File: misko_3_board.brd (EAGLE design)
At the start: 74 x 152 mm, 179 parts, among them IC1 ATMEGA1281-16AU, IC10 ORG1510-MK4, IC11 TPS3808G33DBVT, IC12 LTC4425, IC13 RN-42, IC14 ADXL345, IC15 74HCT1G32, IC16 FM25W256-SOIC, IC17 MICROSD_SPI_MODE, IC18 FH12-30S-0.5SH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

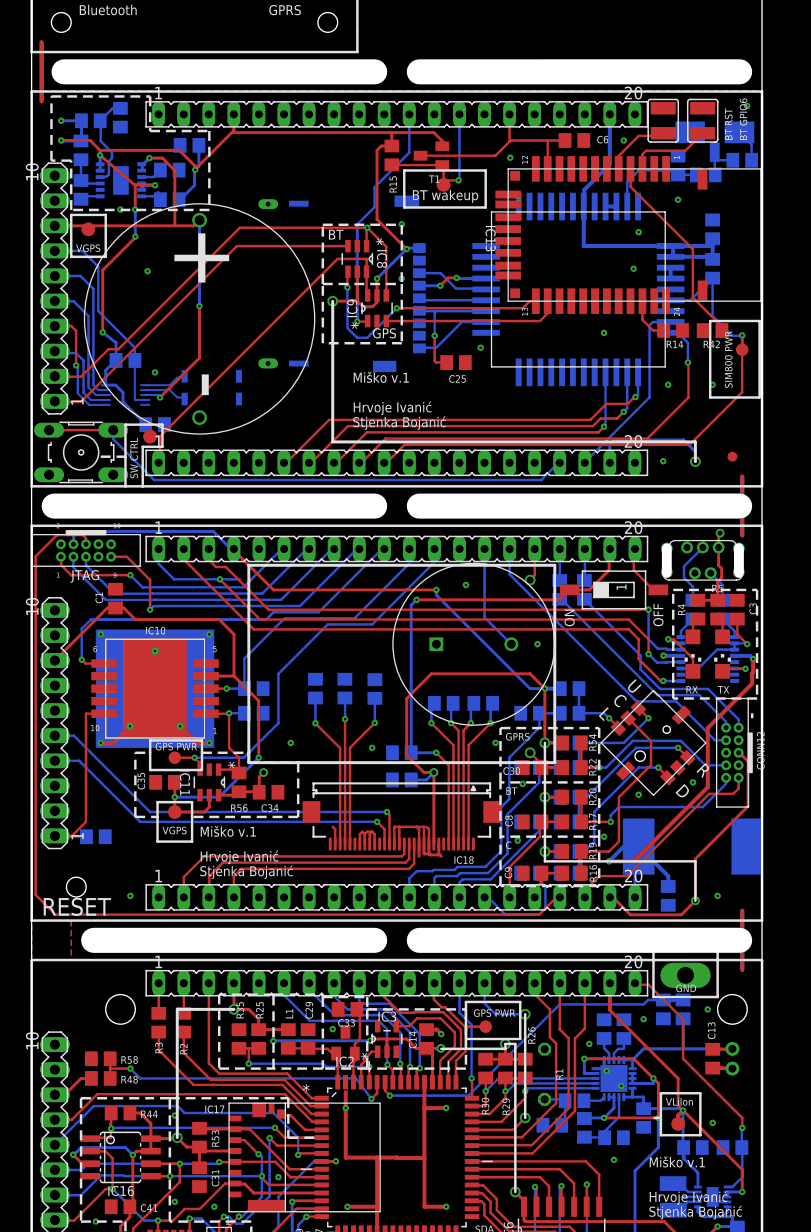
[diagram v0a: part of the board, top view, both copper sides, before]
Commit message: - corrected milling pattern
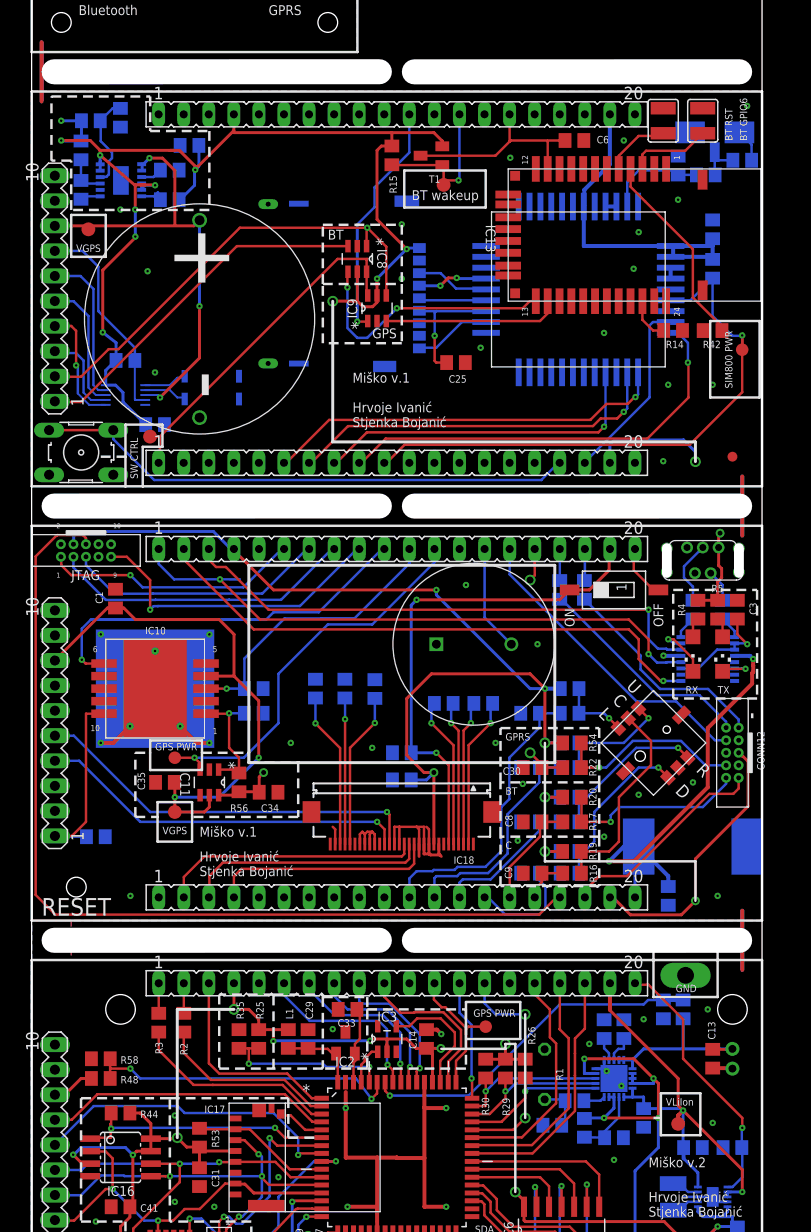
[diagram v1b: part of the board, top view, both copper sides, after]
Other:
- outline, holes or cut-outs redrawn
- board text added: "Miško v.2"

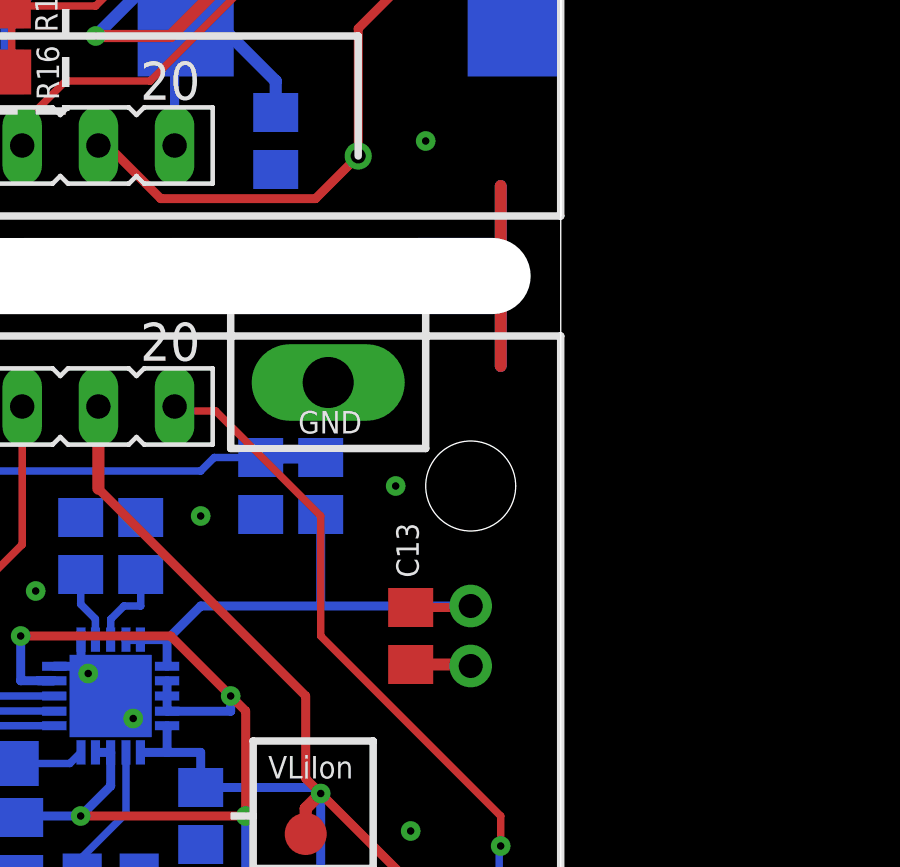
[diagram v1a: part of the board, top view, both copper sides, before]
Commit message: - changed orientation of JST-PH battery connector (--> polarity)
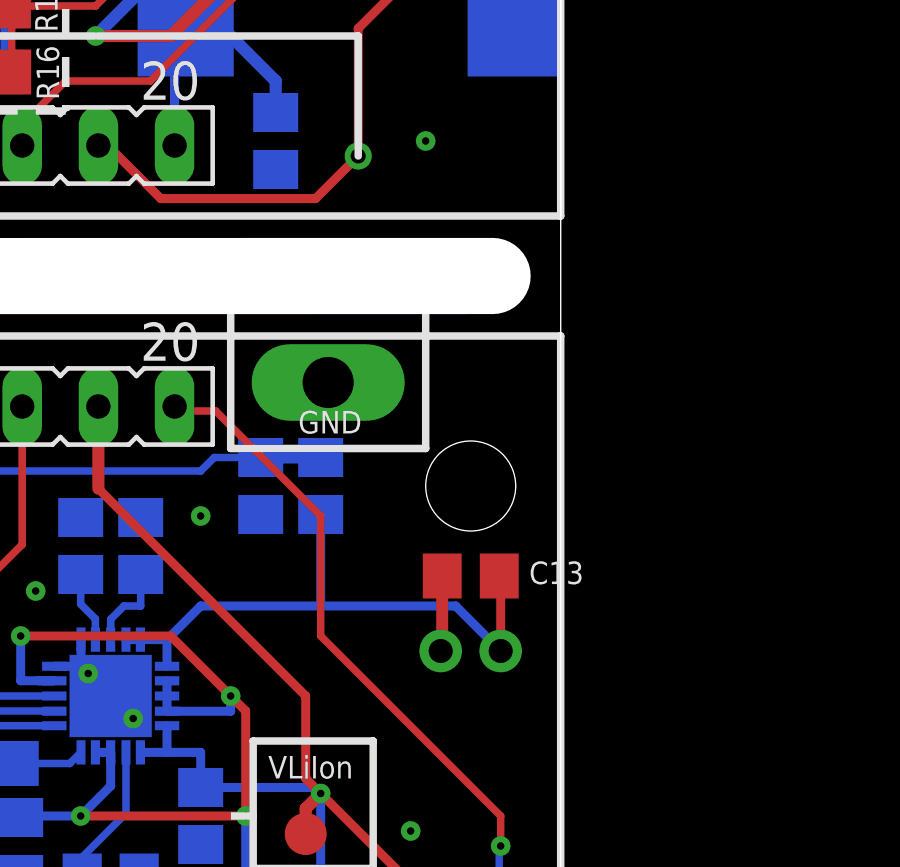
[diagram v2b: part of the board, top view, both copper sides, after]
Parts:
- moved C13 2.83 mm to (71.0, 32.0), turned to 180 degrees
- moved CONN16 0.50 mm to (71.0, 29.5), turned to 180 degrees
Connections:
- net GND: now also CONN16.2; no longer CONN16.1
- net V_LIION+: now also CONN16.1; no longer CONN16.2
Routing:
- net GND: track 133.3 -> 121.8 mm, vias 54 -> 53
- net V_LIION+: track 17.9 -> 20.0 mm
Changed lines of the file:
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@@
 <layer number="24" name="bOrigins" color="15" fill="1" visible="yes" active="yes"/>
 <layer number="25" name="tNames" color="7" fill="1" visible="yes" active="yes"/>
-<layer number="26" name="bNames" color="7" fill="1" visible="yes" active="yes"/>
+<layer number="26" name="bNames" color="7" fill="1" visible="no" active="yes"/>
 <layer number="27" name="tValues" color="7" fill="1" visible="no" active="yes"/>
 <layer number="28" name="bValues" color="7" fill="1" visible="no" active="yes"/>
@@
 <attribute name="VALUE" x="64.54" y="25.27" size="1.27" layer="28" rot="MR270"/>
 </element>
-<element name="C13" library="resistor" package="C0805" value="10µF" x="69" y="30" smashed="yes" rot="R270">
-<attribute name="NAME" x="68.52" y="33.77" size="0.75" layer="25" rot="R270"/>
-<attribute name="VALUE" x="66.46" y="31.27" size="1.27" layer="27" rot="R270"/>
+<element name="C13" library="resistor" package="C0805" value="10µF" x="71" y="32" smashed="yes" rot="R180">
+<attribute name="NAME" x="74.77" y="32.48" size="0.75" layer="25" rot="R180"/>
+<attribute name="VALUE" x="72.27" y="34.54" size="1.27" layer="27" rot="R180"/>
 </element>
 <element name="C14" library="resistor" package="C0805" value="0.1µF" x="40" y="32" smashed="yes" rot="R90">
@@
 <attribute name="VALUE" x="49.48" y="46.26" size="1.27" layer="27"/>
 </element>
-<element name="CONN16" library="SIM800C" package="JST-PH-2-THM-RA" value="LiPo Battery" x="71" y="30" smashed="yes" rot="MR270">
-<attribute name="NAME" x="71.5" y="25.5" size="0.75" layer="26" font="vector" rot="MR0"/>
+<element name="CONN16" library="SIM800C" package="JST-PH-2-THM-RA" value="LiPo Battery" x="71" y="29.5" smashed="yes" rot="MR180">
+<attribute name="NAME" x="75.5" y="30" size="0.75" layer="26" font="vector" rot="MR270"/>
 </element>
 <element name="D1" library="Diode2" package="D0805" value="1N4148" x="28" y="6" smashed="yes">
@@
 <contactref element="R34" pad="1"/>
 <contactref element="C13" pad="1"/>
-<contactref element="CONN16" pad="2"/>
 <wire x1="59.508" y1="29.8796" x2="59.9906" y2="29.8796" width="0.3" layer="16"/>
 <wire x1="59.9906" y1="29.8796" x2="60.8796" y2="29.8796" width="0.3" layer="16"/>
 <wire x1="60.8796" y1="29.8796" x2="60.8796" y2="28.9906" width="0.3" layer="16"/>
-<wire x1="66" y1="31" x2="66" y2="34.05" width="0.3" layer="16"/>
-<wire x1="66" y1="31" x2="71" y2="31" width="0.3" layer="16"/>
+<wire x1="66" y1="34.05" x2="66" y2="31" width="0.3" layer="16"/>
 <wire x1="60.8796" y1="29.8796" x2="62" y2="31" width="0.3" layer="16"/>
 <wire x1="62" y1="31" x2="66" y2="31" width="0.3" layer="16"/>
-<wire x1="69" y1="30.95" x2="71" y2="30.95" width="0.3" layer="1"/>
-<wire x1="71" y1="30.95" x2="71" y2="31" width="0.3" layer="1"/>
+<contactref element="CONN16" pad="1"/>
+<wire x1="66" y1="31" x2="70.5" y2="31" width="0.3" layer="16"/>
+<wire x1="70.5" y1="31" x2="72" y2="29.5" width="0.3" layer="16"/>
+<wire x1="72" y1="29.5" x2="72" y2="31.95" width="0.3" layer="1"/>
+<wire x1="72" y1="31.95" x2="71.95" y2="32" width="0.3" layer="1"/>
 </signal>
 <signal name="VGPS" class="1">
@@
 <contactref element="R32" pad="2"/>
 <contactref element="R1" pad="2"/>
-<contactref element="CONN16" pad="1"/>
 <contactref element="R33" pad="2"/>
 <contactref element="C13" pad="2"/>
@@
 <via x="8.99" y="116.04" extent="1-16" drill="0.25"/>
 <via x="62" y="34" extent="1-16" drill="0.25" diameter="0.4064"/>
-<via x="68.5" y="35" extent="1-16" drill="0.25" diameter="0.4064"/>
 <via x="69" y="23.5" extent="1-16" drill="0.25"/>
 <via x="14.5" y="15.5" extent="1-16" drill="0.25" diameter="0.4064"/>
@@
 <wire x1="72.94" y1="121.04" x2="72.94" y2="122.63" width="0.25" layer="16"/>
 <wire x1="72.94" y1="122.63" x2="71.71" y2="123.86" width="0.25" layer="16"/>
-<wire x1="72" y1="45" x2="72" y2="39" width="0.4" layer="1"/>
-<wire x1="72" y1="45" x2="72" y2="39" width="0.4" layer="16"/>
 <wire x1="72" y1="89" x2="72" y2="83" width="0.4" layer="16"/>
 <wire x1="72" y1="89" x2="72" y2="83" width="0.4" layer="1"/>
@@
 <contactref element="C47" pad="-"/>
 <contactref element="CONN10" pad="2"/>
-<wire x1="69" y1="29.05" x2="71" y2="29.05" width="0.4" layer="1"/>
-<wire x1="71" y1="29.05" x2="71" y2="29" width="0.4" layer="1"/>
+<contactref element="CONN16" pad="2"/>
+<wire x1="70.05" y1="32" x2="70.05" y2="29.55" width="0.4" layer="1"/>
+<wire x1="70.05" y1="29.55" x2="70" y2="29.5" width="0.4" layer="1"/>
 <wire x1="135" y1="45.43" x2="147" y2="45.43" width="0" layer="19" extent="1-1"/>
 <wire x1="123" y1="45.43" x2="135" y2="45.43" width="0" layer="19" extent="1-1"/>
 <wire x1="111" y1="45.43" x2="123" y2="45.43" width="0" layer="19" extent="1-1"/>
 <wire x1="99" y1="45.43" x2="111" y2="45.43" width="0" layer="19" extent="1-1"/>
-<wire x1="72" y1="45" x2="99" y2="45.43" width="0" layer="19" extent="16-16"/>
+<wire x1="69.5" y1="46.5" x2="99" y2="45.43" width="0" layer="19" extent="1-1"/>
 <wire x1="49.55" y1="59.5" x2="49.8" y2="59.5" width="0" layer="19" extent="1-16"/>
-<wire x1="59" y1="28" x2="59.75" y2="27.25" width="0" layer="19" extent="16-16"/>
 <wire x1="49.55" y1="48.8" x2="49.25" y2="52.1" width="0" layer="19" extent="16-16"/>
 <wire x1="49.8" y1="48.8" x2="49.55" y2="48.8" width="0" layer="19" extent="1-16"/>
+<wire x1="66.25" y1="38.45" x2="64.5" y2="45.55" width="0" layer="19" extent="16-16"/>
+<wire x1="59" y1="28" x2="59.75" y2="27.25" width="0" layer="19" extent="16-16"/>
 </signal>
 <signal name="GPRS_LED" class="2">

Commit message: - bill of materials in csv format - unified voltage divider resistors - corrected capacitor value 100nF -> 0.1µF
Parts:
- C10: value 100nF -> 0.1µF
- R25, R35: value 200k -> 150k
- R37, R38: value 100k -> 150k
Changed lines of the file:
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@@
 <attribute name="VALUE" x="58.365" y="24.54" size="1.27" layer="28" rot="MR180"/>
 </element>
-<element name="R25" library="rcl" package="R0805" value="200k" x="23" y="32" smashed="yes" rot="R270">
+<element name="R25" library="rcl" package="R0805" value="150k" x="23" y="32" smashed="yes" rot="R270">
 <attribute name="NAME" x="23.5" y="34" size="0.75" layer="25" rot="R90"/>
 <attribute name="VALUE" x="20.46" y="32.635" size="1.27" layer="27" rot="R270"/>
@@
 <attribute name="VALUE" x="63.46" y="34.365" size="1.27" layer="28" rot="MR90"/>
 </element>
-<element name="R35" library="rcl" package="R0805" value="200k" x="21" y="32" smashed="yes" rot="R90">
+<element name="R35" library="rcl" package="R0805" value="150k" x="21" y="32" smashed="yes" rot="R90">
 <attribute name="NAME" x="21.5" y="34" size="0.75" layer="25" rot="R90"/>
 <attribute name="VALUE" x="23.54" y="31.365" size="1.27" layer="27" rot="R90"/>
@@
 <attribute name="VALUE" x="21.865" y="67.54" size="1.27" layer="28" rot="MR180"/>
 </element>
-<element name="R37" library="resistor" package="R0805" value="100k" x="4.99" y="118.04" smashed="yes" rot="MR90">
+<element name="R37" library="resistor" package="R0805" value="150k" x="4.99" y="118.04" smashed="yes" rot="MR90">
 <attribute name="NAME" x="6.25" y="117" size="0.75" layer="26" rot="MR90"/>
 <attribute name="VALUE" x="2.45" y="117.405" size="1.27" layer="28" rot="MR90"/>
 </element>
-<element name="R38" library="resistor" package="R0805" value="100k" x="4.99" y="122.04" smashed="yes" rot="MR90">
+<element name="R38" library="resistor" package="R0805" value="150k" x="4.99" y="122.04" smashed="yes" rot="MR90">
 <attribute name="NAME" x="6.25" y="121.25" size="0.75" layer="26" rot="MR90"/>
 <attribute name="VALUE" x="2.45" y="121.405" size="1.27" layer="28" rot="MR90"/>
@@
 <attribute name="NAME" x="67.5" y="51" size="0.75" layer="22" rot="MR0"/>
 </element>
-<element name="C10" library="resistor" package="C0805" value="100nF" x="64.5" y="46.5" smashed="yes" rot="MR90">
+<element name="C10" library="resistor" package="C0805" value="0.1µF" x="64.5" y="46.5" smashed="yes" rot="MR90">
 <attribute name="NAME" x="65.77" y="45.73" size="0.75" layer="26" rot="MR90"/>
 <attribute name="VALUE" x="61.96" y="45.23" size="1.27" layer="28" rot="MR90"/>
